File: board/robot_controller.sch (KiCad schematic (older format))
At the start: 131 parts, among them J101 CONN_2, J102 CONN_2, J103 CONN_2, J104 CONN_2, J105 JTAG-ARM, J106 CONN_2, J107 USBCONN, J108 CONN_8, J109 CONN_8, J110 USBCONN, J111 CONN_4, P101 CONN_1, P102 CONN_1, P103 CONN_1, P104 CONN_1, P105 CONN_1, P106 CONN_1, P107 CONN_1, P108 CONN_1, P109 CONN_1, P110 CONN_1, P111 CONN_1, P112 CONN_1, P113 CONN_1, P114 CONN_1, P115 CONN_1, P116 CONN_1, P117 CONN_1, P118 CONN_1, P119 CONN_1, P120 CONN_1, P121 CONN_1, P122 CONN_1, P123 CONN_1, P124 CONN_1, P125 CONN_1, P126 CONN_1, P127 CONN_1, P128 CONN_1, P129 CONN_1, Q101 PNP, SW101 SPST, SW102 SPST, SW103 SPST, SW104 SPST, SW105 SPST, SW106 SPST, U101 STM32F405-144, U102 FT232RL, X101 8MHZ

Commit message: Selected Part Numbers for all Components
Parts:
- removed C110, C127, C130: 100nF, symbol C
- removed J101: CONN_2, symbol CONN_2
- added C108: 100uF, symbol CP1
- added C125, C126, C132: 100nF, symbol C
- added C135: 2.2uF, symbol C
- added P101: CONN_4, symbol CONN_4
- C101, C102, C103, C104: Part Number (none) -> CL10A106MQ8NNNC
- C105, C106: Part Number (none) -> CL10C180JC8NNNC
- C107, C111, C112, C113, C114, C115, C116, C117, C118, C119, C120, C121, C122, C123, C124, C129, C131: Part Number (none) -> CL10F104ZA8NNNC
- C109: Part Number (none) -> CGA3E3X7S2A104K080AB
- C110: renamed from C108; Part Number (none) -> CL10F104ZA8NNNC
- C127: renamed from C125; Part Number (none) -> CL10F105ZP8NNNC
- C128: renamed from C126; Part Number (none) -> C1608X7R2A103K080AA
- C130: renamed from C128; Part Number (none) -> CL10A475KQ8NNNC
- C133: value 2.2uF -> 100nF; Part Number (none) -> CL10F104ZA8NNNC
- C134: renamed from C132; Part Number (none) -> CL10A225KQ8NNNC
- C136: renamed from C134; Part Number (none) -> CL10B333KB8SFNC
- J101: renamed from J102; Part Number (none) -> 1716020000
- J102: renamed from J103; Part Number (none) -> 1716020000
- J103: renamed from J104; Part Number (none) -> 1716020000
- J105: renamed from J106; Part Number (none) -> ESPM02200
- J107: renamed from J108; Part Number (none) -> 9993960000
- J108: renamed from J109; Part Number (none) -> 9993960000
- J110: renamed from J111; Part Number (none) -> HEADER
- JP101, JP102, JP103: Part Number (none) -> JUMPER
- Q101: Part Number (none) -> 2SA10220CL
- R101, R102, R104, R106, R107: Part Number (none) -> RC1608J101CS
- R103, R105: Part Number (none) -> RC1608J102CS
- R108, R109, R110, R111, R112, R113, R114, R115, R116, R117, R118, R119, R120, R124: Part Number (none) -> RC1608J103CS
- R121: Part Number (none) -> RC1608J221CS
- R122: Part Number (none) -> MCR03ERTF1502
- R123: value 320 -> 316; Part Number (none) -> RC1608F3160CS
- R125: Part Number (none) -> MCR03ERTF1101
- R126: value 3.1k -> 3.3k; Part Number (none) -> MCR50JZHJ332
- R128: Part Number (none) -> RC1608J821CS
- R129, R130, R131, R132: Part Number (none) -> RC1608J472CS
- U102: Part Number (none) -> FT232RL
- renumbered J105 to J104, J107 to J106, J110 to J109, P101 to P102, P102 to P103, P103 to P104, P104 to P105, P105 to P106, P106 to P107, P107 to P108, P108 to P109, P109 to P110, P110 to P111, P111 to P112, P112 to P113, P113 to P114, P114 to P115, P115 to P116, P116 to P117, P117 to P118, P118 to P119, P119 to P120, P120 to P121, P121 to P122, P122 to P123, P123 to P124, P124 to P125, P125 to P126, P126 to P127, P127 to P128, P128 to P129, P129 to P130
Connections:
- net +24V: now also C109.1, C108.1
- net +3.3V: now also C125.1, C126.1, C132.1; no longer C109.1
- net +5V: now also C131.1; no longer C129.1
- net GND: now also C125.2, C126.2, C132.2, C135.2, P101.3 (P3), P101.4 (P4); no longer C109.2
- net GNDPWR: now also C109.2, C108.2
- net LED Data 0/DATA_OUT: now also P101.1 (P1)
- net LED Data 1/DATA_OUT: now also P101.2 (P2)
- net SUPPLY_SENSE: now also C129.1
- net VCAP2: now also C135.1; no longer C133.1
- net at U102.17 (3V3OUT): now also C133.1; no longer C131.1
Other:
- moved on the sheet: J105, JP101

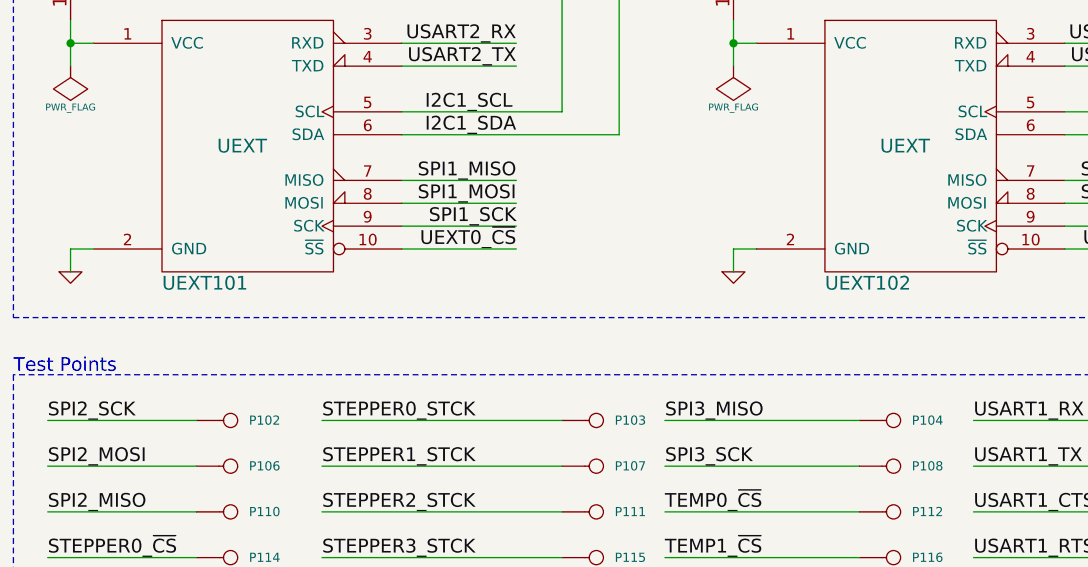
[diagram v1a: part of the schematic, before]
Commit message: Industrial Output Ground, Associated Footprints
* Fixed an issue with the industrial output ground, it is now on the
  power ground rail.
* Associated most of the footprints, need to make a few.
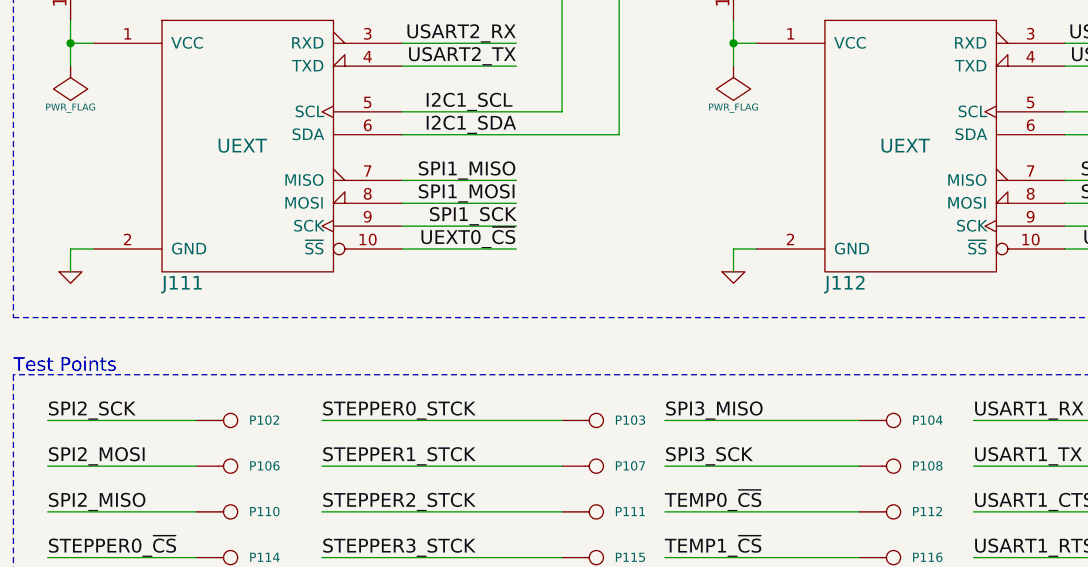
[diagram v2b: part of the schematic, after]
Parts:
- renumbered UEXT101 to J111, UEXT102 to J112
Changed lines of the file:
@@
 $EndComp
 $Comp
-L UEXT UEXT102
+L UEXT J112
 U 1 1 530D497E
 P 24800 22500
-F 0 "UEXT102" H 24450 21900 60  0000 L CNN
+F 0 "J112" H 24450 21900 60  0000 L CNN
 F 1 "UEXT" H 24800 22500 60  0000 C CNN
 F 2 "" H 25400 22650 60  0000 C CNN
@@
 $EndComp
 $Comp
-L UEXT UEXT101
+L UEXT J111
 U 1 1 530D51C7
 P 21900 22500
-F 0 "UEXT101" H 21550 21900 60  0000 L CNN
+F 0 "J111" H 21550 21900 60  0000 L CNN
 F 1 "UEXT" H 21900 22500 60  0000 C CNN
 F 2 "" H 22500 22650 60  0000 C CNN

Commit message: Digikey Number + Link
Added a digikey part number and link to all components.
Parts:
- C101, C102, C103, C104: Digikey Number (none) -> 1276-1119-1-ND; Part Number CL10A106MQ8NNNC -> (none)
- C105, C106: Digikey Number (none) -> 1276-2210-1-ND; Part Number CL10C180JC8NNNC -> (none)
- C107, C110, C111, C112, C113, C114, C115, C116, C117, C118, C119, C120, C121, C122, C123, C124, C125, C126, C129, C131, C132, C133: Digikey Number (none) -> 1276-1011-1-ND; Part Number CL10F104ZA8NNNC -> (none)
- C108: Digikey Number (none) -> P13622-ND; Part Number EEU-EE2C101 -> (none)
- C109: Digikey Number (none) -> 445-6938-1-ND; Part Number CGA3E3X7S2A104K080AB -> (none)
- C127: Digikey Number (none) -> 1276-1041-1-ND; Part Number CL10F105ZP8NNNC -> (none)
- C128: Digikey Number (none) -> 445-1304-1-ND; Part Number C1608X7R2A103K080AA -> (none)
- C130: Digikey Number (none) -> 1276-1045-1-ND; Part Number CL10A475KQ8NNNC -> (none)
- C134, C135: Digikey Number (none) -> 1276-1183-1-ND; Part Number CL10A225KQ8NNNC -> (none)
- C136: Digikey Number (none) -> 1276-2042-1-ND; Part Number CL10B333KB8SFNC -> (none)
- D101, D102, D103, D104: Digikey Number (none) -> 475-2815-1-ND; Part Number LB Q39E-N1P1-35-1 -> (none)
- D105: Digikey Number (none) -> 475-2832-1-ND; Part Number LW Q38G-Q1S1-3K6L-1 -> (none)
- D106: Digikey Number (none) -> 67-1693-1-ND; Part Number SML-LX0603SUGW-TR -> (none)
- D107: Digikey Number (none) -> 67-1551-1-ND; Part Number SML-LX0603SRW-TR -> (none)
- D108, D109: Digikey Number (none) -> CD0603-Z3V3CT-ND; Part Number CD0603-Z3V3 -> (none)
- J101, J102, J103: Digikey Number (none) -> 281-1435-ND; Part Number 1716020000 -> (none)
- J104: Digikey Number (none) -> ED10524-ND; Part Number 302-S201 -> (none)
- J105: Digikey Number (none) -> APC1274-ND; Part Number ESPM02200 -> (none)
- J106, J109: Digikey Number (none) -> ED2983-ND; Part Number USB-B1HSB6 -> (none)
- J107, J108: Digikey Number (none) -> 281-1439-ND; Part Number 9993960000 -> (none)
- J110: Digikey Number (none) -> S1011EC-40-ND; Part Number HEADER -> (none)
- J111, J112: Digikey Number (none) -> ED1543-ND; Part Number 302-S101 -> (none)
- JP101, JP102, JP103: Part Number JUMPER -> (none)
- L101: Digikey Number (none) -> 445-6150-1-ND; Part Number GLFR1608T101M-LR -> (none)
- P101: Digikey Number (none) -> 281-1437-ND; Part Number 9993920000 -> (none)
- P102, P103, P104, P105, P106, P107, P108, P109, P110, P111, P112, P113, P114, P115, P116, P117, P118, P119, P120, P121, P122, P123, P124, P125, P126, P127, P128, P129, P130: Digikey Number (none) -> 5001K-ND; Part Number 5001K-ND -> (none)
- Q101: Digikey Number (none) -> 2SA10220CLCT-ND; Part Number 2SA10220CL -> (none)
- R101, R102, R104, R106, R107: Digikey Number (none) -> 1276-5038-1-ND; Part Number RC1608J101CS -> (none)
- R103, R105: Digikey Number (none) -> 1276-5062-1-ND; Part Number RC1608J102CS -> (none)
- R108, R109, R110, R111, R112, R113, R114, R115, R116, R117, R118, R119, R120, R124: Digikey Number (none) -> 1276-5086-1-ND; Part Number RC1608J103CS -> (none)
- R121: Digikey Number (none) -> 1276-5046-1-ND; Part Number RC1608J221CS -> (none)
- R122: Digikey Number (none) -> RHM15.0KCFCT-ND; Part Number MCR03ERTF1502 -> (none)
- R123: Digikey Number (none) -> 1276-4602-1-ND; Part Number RC1608F3160CS -> (none)
- R125: Digikey Number (none) -> RHM1.1KCFCT-ND; Part Number MCR03ERTF1101 -> (none)
- R126: Digikey Number (none) -> RHM3.3KBGCT-ND; Part Number MCR50JZHJ332 -> (none)
- R127: Digikey Number (none) -> A105820-ND; Part Number 1630480-9 -> (none)
- R128: Digikey Number (none) -> 1276-5060-1-ND; Part Number RC1608J821CS -> (none)
- R129, R130, R131, R132: Digikey Number (none) -> 1276-5078-1-ND; Part Number RC1608J472CS -> (none)
- SW101, SW102, SW103, SW104, SW105, SW106: Digikey Number (none) -> 450-1650-ND; Part Number FSM4JH -> (none)
- U101: Digikey Number (none) -> 497-11909-ND; Part Number STM32F405ZGT6 -> (none)
- U102: Digikey Number (none) -> 768-1007-1-ND; Part Number FT232RL -> (none)
- X101: Digikey Number (none) -> 887-1263-1-ND; Part Number 9C-8.000MEEJ-T -> (none)

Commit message: Removed PWR-GND, change footprint for a bunch of capacitors
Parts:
- removed JP101: JUMPER, symbol JUMPER
- C109: Digikey Number 445-6938-1-ND -> 399-6753-1-ND
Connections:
- net GNDPWR is gone; now on net GND: C108.2, C109.2, J105.2 (PM)
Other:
- moved on the sheet: C101, C102, C103, C104, C105, C106, C107, C108, C109, C110, C111, C112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

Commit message: Layed out in general where stuff is going to be located.
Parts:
- renumbered P101 to J113
